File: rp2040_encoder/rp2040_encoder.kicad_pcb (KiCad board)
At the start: 2 copper layers, 35.9 x 32.8 mm, 14 parts, among them J1 Conn_01x05, U1 MT6701, U2 love

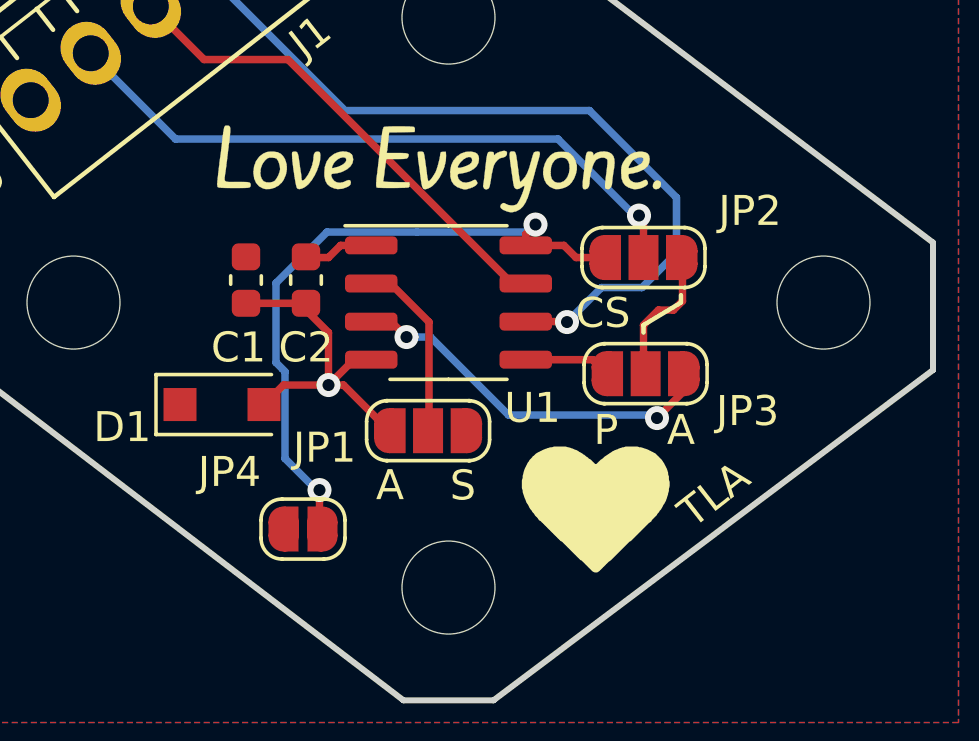
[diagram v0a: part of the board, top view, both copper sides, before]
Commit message: updated design with dual CPUs
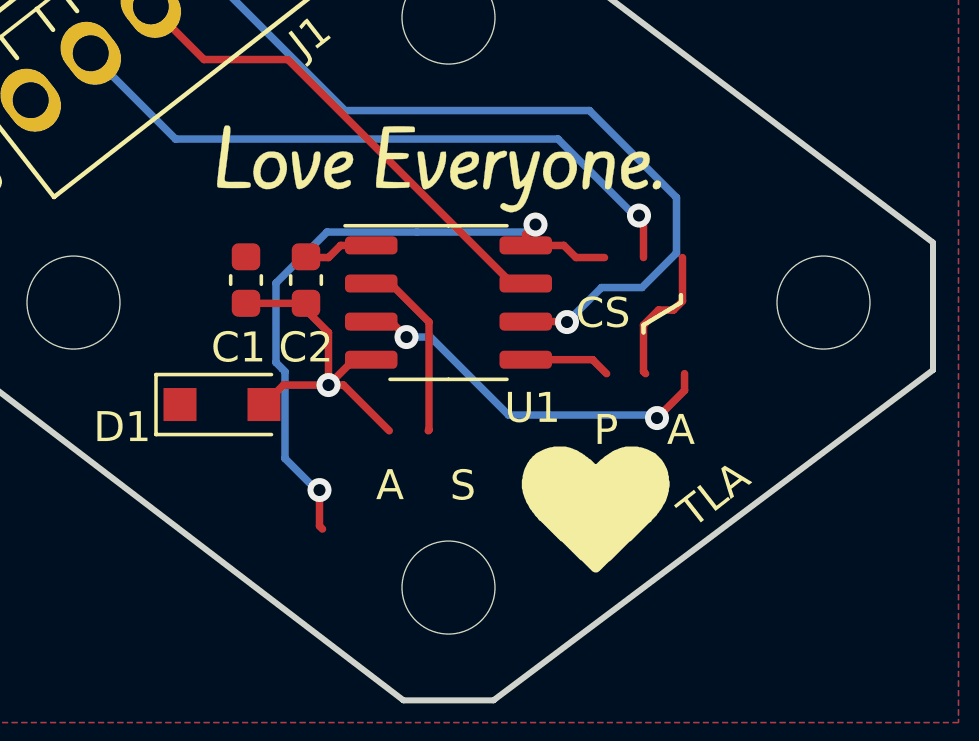
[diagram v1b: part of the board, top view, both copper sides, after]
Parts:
- removed JP1, JP2, JP3: SolderJumper_3_Open, Jumper:SolderJumper-3_P1.3mm_Open_RoundedPad1.0x1.5mm_NumberLabels
- removed JP4: SolderJumper_2_Open, Jumper:SolderJumper-2_P1.3mm_Open_RoundedPad1.0x1.5mm
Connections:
- U1 pad 2: Net-(JP1-Pad2) -> +3V3
- U1 pad 3: Net-(JP3-Pad3) -> unconnected-(U1-Pad3)
- U1 pad 5: Net-(JP3-Pad1) -> unconnected-(U1-Pad5)
- U1 pad 8: Net-(JP4-Pad2) -> unconnected-(U1-Pad8)
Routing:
- net unconnected-(U1-Pad8): track 0.00 -> 22.0 mm, vias 0 -> 2
- net Net-(JP4-Pad2): track 22.0 -> 0.00 mm, vias 2 -> 0
- net unconnected-(U1-Pad3): track 0.00 -> 12.7 mm, vias 0 -> 2
- net Net-(JP3-Pad3): track 12.7 -> 0.00 mm, vias 2 -> 0
- net Net-(JP1-Pad2): track 6.09 -> 0.00 mm
- net +3V3: track 2.35 -> 8.45 mm
- net Net-(JP3-Pad2): track 4.73 -> 0.00 mm
- net (no net): track 0.00 -> 4.73 mm
- net unconnected-(U1-Pad5): track 0.00 -> 2.89 mm
- net Net-(JP3-Pad1): track 2.89 -> 0.00 mm

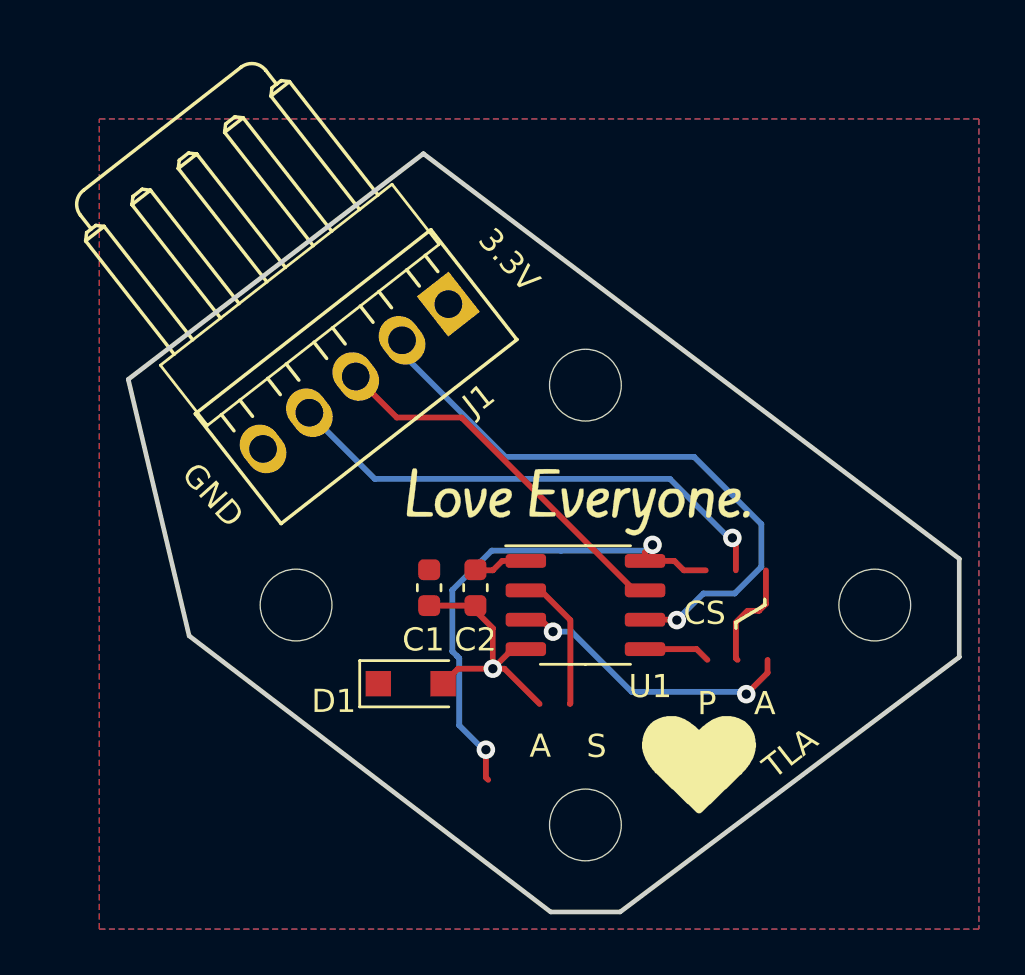
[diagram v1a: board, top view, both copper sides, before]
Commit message: Add encoder, update readme
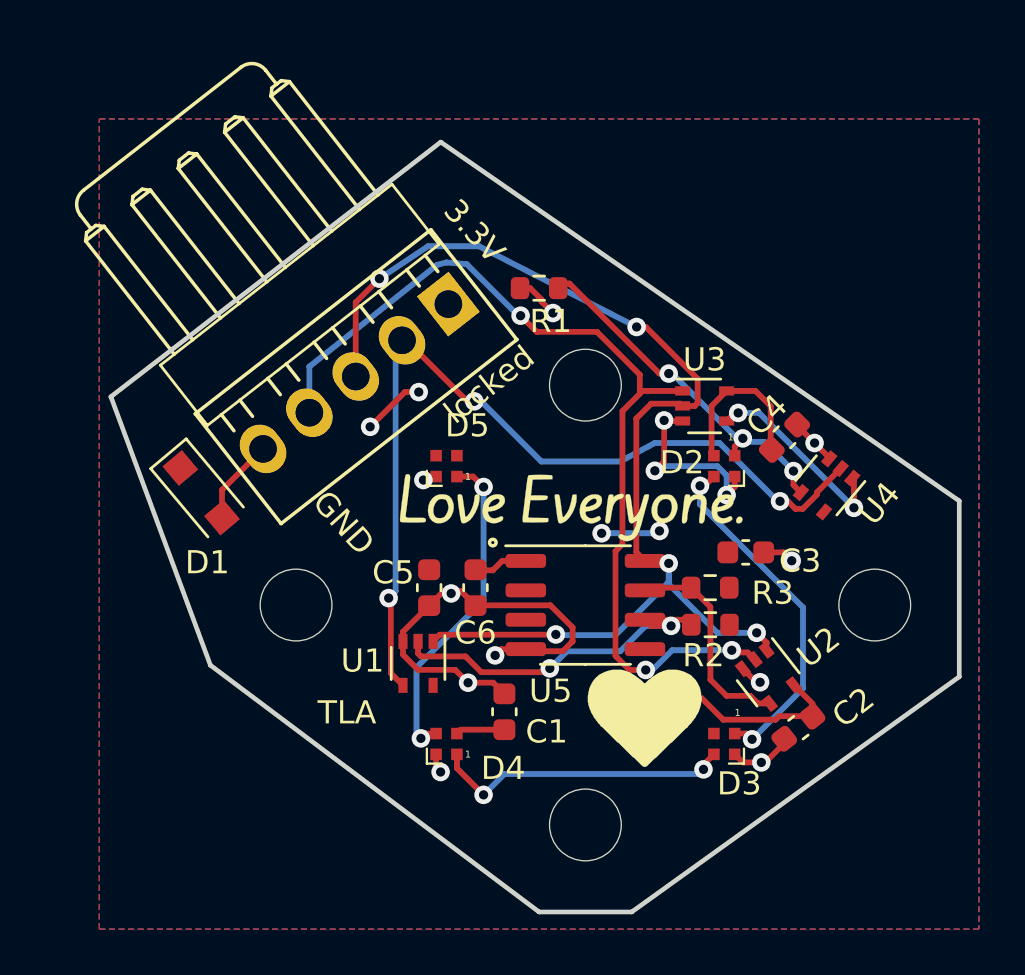
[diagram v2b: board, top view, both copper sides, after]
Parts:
- added C1: 0.1uF, Capacitor_SMD:C_0603_1608Metric, F.Cu at (146.5, 104.6)
- added C2: 0.1uF, Capacitor_SMD:C_0603_1608Metric, F.Cu at (159.2, 105.3)
- added C3: 0.1uF, Capacitor_SMD:C_0603_1608Metric, F.Cu at (156.9, 97.7)
- added C4: 0.1uF, Capacitor_SMD:C_0603_1608Metric, F.Cu at (158.6, 92.8)
- added D2: SK6805, LED_SMD:LED_SK6812_EC15_1.5x1.5mm, F.Cu at (156.0, 94.0)
- added D3: SK6805, LED_SMD:LED_SK6812_EC15_1.5x1.5mm, F.Cu at (156.0, 106.0)
- added D4: SK6805, LED_SMD:LED_SK6812_EC15_1.5x1.5mm, F.Cu at (144.0, 106.0)
- added D5: SK6805, LED_SMD:LED_SK6812_EC15_1.5x1.5mm, F.Cu at (144.0, 94.0)
- added R1: 10k, Resistor_SMD:R_0603_1608Metric, F.Cu at (148.0, 86.3)
- added R2: 10k, Resistor_SMD:R_0603_1608Metric, F.Cu at (155.4, 100.8)
- added R3: 10k, Resistor_SMD:R_0603_1608Metric, F.Cu at (155.4, 99.2)
- added U1: SN74LVC1G07QDCKTQ1, Package_TO_SOT_SMD:SOT-353_SC-70-5, F.Cu at (142.8, 102.5)
- added U2: SN74LVC1G07QDCKTQ1, Package_TO_SOT_SMD:SOT-353_SC-70-5, F.Cu at (157.9, 103.1)
- added U3: SN74LVC1G79DBVR, Package_TO_SOT_SMD:SOT-353_SC-70-5, F.Cu at (155.2, 91.4)
- added U4: SN74LVC1G07QDCKTQ1, Package_TO_SOT_SMD:SOT-353_SC-70-5, F.Cu at (160.4, 94.8)
- moved D1 12.2 mm to (133.4, 95.2), turned to -50 degrees
- moved Logo1 0.39 mm to (149.4, 95.7)
- renumbered C1 to C5, C2 to C6, U2 to Logo1, U1 to U5, J1 to locked
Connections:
- U5 pad 6: SPI0RX/A -> DO
- U5 pad 7: SPI0CS/B -> SCK
- U5 pad 8: unconnected-(U1-Pad8) -> SPI0CS/B
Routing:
- net SPI0CS/B: track 16.8 -> 50.6 mm, vias 0 -> 5
- net GND: track 11.9 -> 45.1 mm, vias 1 -> 15
- net unconnected-(U1-Pad8): track 22.0 -> 0.00 mm, vias 2 -> 0
- net SPI0SCK/C: track 22.0 -> 41.1 mm, vias 1 -> 3
- net DO: track 0.00 -> 16.3 mm, vias 0 -> 2
- net Net-(D2-Pad3): track 0.00 -> 15.4 mm, vias 0 -> 2
- net LED: track 0.00 -> 15.1 mm, vias 0 -> 3
- net Net-(D4-Pad3): track 0.00 -> 14.2 mm, vias 0 -> 2
- net Net-(D3-Pad3): track 0.00 -> 13.0 mm, vias 0 -> 2
- net +3V3: track 8.45 -> 21.2 mm, vias 0 -> 2
- net unconnected-(U5-Pad3): track 12.7 -> 0.00 mm, vias 2 -> 0
- net SPI0RX/A: track 27.0 -> 38.9 mm, vias 1 -> 3
- net SCK: track 0.00 -> 9.36 mm
- net Net-(U3-Pad4): track 0.00 -> 8.65 mm, vias 0 -> 2
- net (no net): track 4.73 -> 0.00 mm
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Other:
- board size 35.9 x 32.8 mm -> 36.7 x 33.3 mm
- board text removed: "A"
- board text removed: "CS"
- board text removed: "P"
- board text removed: "S"

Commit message: Update boards for latest build, pending design review.
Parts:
- removed C1, C2, C3, C4: 0.1uF, Capacitor_SMD:C_0603_1608Metric
- removed D2, D3, D4, D5: SK6805, LED_SMD:LED_SK6812_EC15_1.5x1.5mm
- removed U1, U2, U4: SN74LVC1G07QDCKTQ1, Package_TO_SOT_SMD:SOT-353_SC-70-5
- removed U3: SN74LVC1G79DBVR, Package_TO_SOT_SMD:SOT-353_SC-70-5
- removed locked: Conn_01x05, parts:Molex_KK-254_1x05_P2.54mm_Horizontal
- added J1: Conn_01x02, Connector_PinHeader_2.54mm:PinHeader_1x02_P2.54mm_Vertical, F.Cu at (158.8, 93.8)
- added J2: Conn_01x06, parts:Molex_KK-254_1x06_P2.54mm_Horizontal, F.Cu at (144.8, 86.3)
- added TH1: Thermistor 10k, Resistor_SMD:R_0603_1608Metric, F.Cu at (150.2, 103.8)
- R1, R2, R3: value 10k -> 100R
- moved R1 13.9 mm to (155.4, 98.0)
- moved D1 13.3 mm to (143.8, 103.5), turned to 0 degrees
- moved R3 1.93 mm to (155.4, 101.2)
- moved R2 1.26 mm to (155.4, 99.6)
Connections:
- R1 pad 1: LED -> Net-(J2-Pin_3)
- R1 pad 2: GND -> SPI0CS/B
- R2 pad 1: +3V3 -> Net-(J2-Pin_4)
- R2 pad 2: DO -> SPI0SCK/C
- R3 pad 1: +3V3 -> Net-(J2-Pin_2)
- R3 pad 2: SCK -> SPI0RX/A
- U5 pad 6: DO -> SPI0RX/A
- U5 pad 7: SCK -> SPI0SCK/C
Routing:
- net /TH1_SENSE: track 0.00 -> 52.1 mm, vias 0 -> 1
- net SPI0CS/B: track 50.6 -> 2.07 mm, vias 5 -> 0
- net SPI0SCK/C: track 41.1 -> 2.14 mm, vias 3 -> 0
- net GND: track 45.1 -> 8.01 mm, vias 15 -> 3
- net SPI0RX/A: track 38.9 -> 2.27 mm, vias 3 -> 0
- net Net-(J2-Pin_4): track 0.00 -> 25.8 mm
- net Net-(J2-Pin_2): track 0.00 -> 23.4 mm
- net +3V3: track 21.2 -> 0.00 mm, vias 2 -> 0
- net Net-(J2-Pin_3): track 0.00 -> 19.0 mm
- net DO: track 16.3 -> 0.00 mm, vias 2 -> 0
- net Net-(D2-Pad3): track 15.4 -> 0.00 mm, vias 2 -> 0
- net LED: track 15.1 -> 0.00 mm, vias 3 -> 0
- net Net-(D4-Pad3): track 14.2 -> 0.00 mm, vias 2 -> 0
- net Net-(D3-Pad3): track 13.0 -> 0.00 mm, vias 2 -> 0
- net SCK: track 9.36 -> 0.00 mm
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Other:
- board text added: "Designed by Sequoia Hope Alexander for you"
- board text added: "SHA"
- board text removed: "Designed by Taylor Alexander for you"
- board text removed: "TLA"

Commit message: Updated files for boards ordered July 2024
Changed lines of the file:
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@@
 	)
 	(paper "A4")
+	(title_block
+		(title "rp2040_encoder")
+	)
 	(layers
 		(0 "F.Cu" signal)
@@
 			(net 6 "unconnected-(U5-OUT-Pad3)")
 			(pinfunction "OUT")
-			(pintype "output")
+			(pintype "output+no_connect")
 		)
 		(pad "4" smd roundrect
@@
 			(net 7 "unconnected-(U5-PUSH-Pad5)")
 			(pinfunction "PUSH")
-			(pintype "output")
+			(pintype "output+no_connect")
 		)
 		(pad "6" smd roundrect
@@
 	)
 	(gr_circle
-		(center 142.5 95)
-		(end 142.5 94.5)
+		(center 150 100)
+		(end 150 99.5)
 		(stroke
 			(width 0.1)
@@
 	)
 	(segment
-		(start 144 82.5)
-		(end 143 82.5)
+		(start 136.188362 95.5)
+		(end 134.837263 94.148901)
 		(width 0.2)
 		(layer "B.Cu")
@@
 	)
 	(segment
-		(start 136.188362 95.5)
-		(end 134.837263 94.148901)
+		(start 156.879248 92.192319)
+		(end 151.836929 87.15)
 		(width 0.2)
 		(layer "B.Cu")
@@
 	)
 	(segment
-		(start 148.65 87.15)
-		(end 144 82.5)
+		(start 149.15 87.15)
+		(end 144.5 82.5)
 		(width 0.2)
 		(layer "B.Cu")
@@
 	)
 	(segment
-		(start 148.5 104.5)
-		(end 146.61005 104.5)
+		(start 134.837263 90.662737)
+		(end 134.837263 94.148901)
 		(width 0.2)
 		(layer "B.Cu")
@@
 	)
 	(segment
-		(start 143 82.5)
-		(end 134.837263 90.662737)
+		(start 151.836929 87.15)
+		(end 149.15 87.15)
 		(width 0.2)
 		(layer "B.Cu")
@@
 	)
 	(segment
-		(start 156.879248 92.192319)
-		(end 151.836929 87.15)
+		(start 144.5 82.5)
+		(end 143 82.5)
 		(width 0.2)
 		(layer "B.Cu")
@@
 	)
 	(segment
-		(start 134.837263 90.662737)
-		(end 134.837263 94.148901)
+		(start 143 82.5)
+		(end 134.837263 90.662737)
+		(width 0.2)
+		(layer "B.Cu")
+		(net 11)
+	)
+	(segment
+		(start 148.5 104.5)
+		(end 146.61005 104.5)
 		(width 0.2)
 		(layer "B.Cu")
@@
 		(width 0.2)
 		(layer "B.Cu")
-		(net 11)
-	)
-	(segment
-		(start 151.836929 87.15)
-		(end 148.65 87.15)
-		(width 0.2)
-		(layer "B.Cu")
